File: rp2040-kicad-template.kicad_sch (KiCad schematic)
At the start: 47 parts, among them U1 RP2040, U2 TYPE-C-31-M-12, U3 XC6206PxxxMR, U5 USB Boot, U6 Reset, U7 W25Q16JVUXIQ, U8 PJ-320A, Y1 12MHz - 20pF

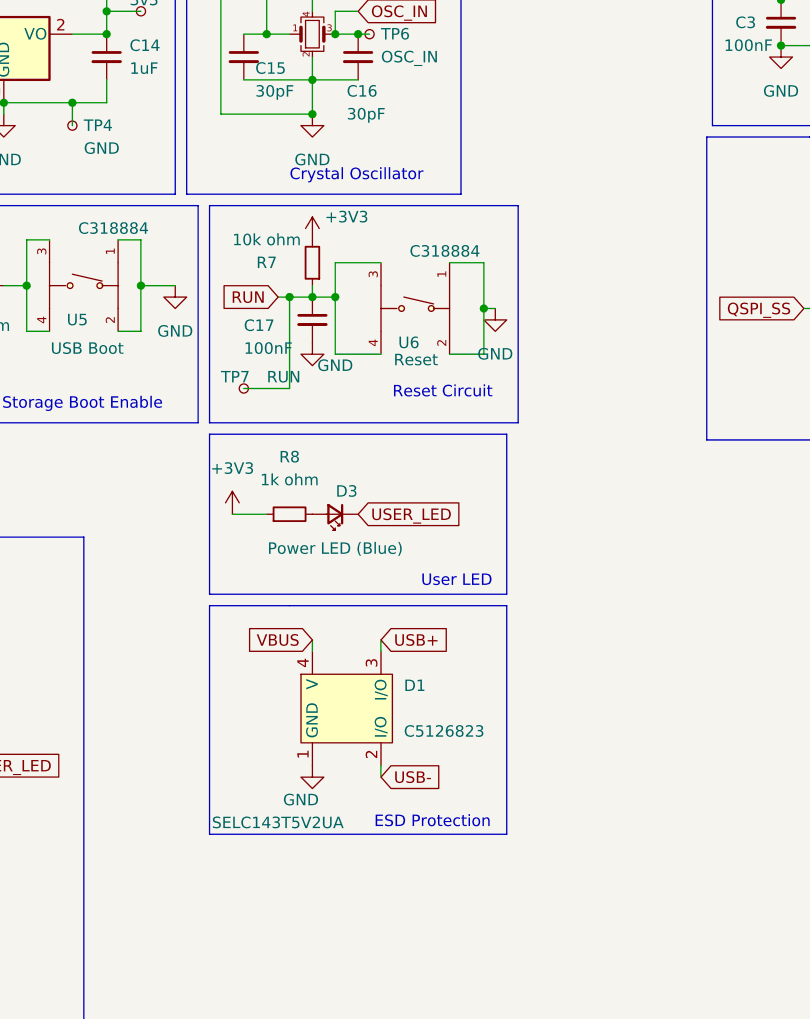
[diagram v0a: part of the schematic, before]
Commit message: Add a different ESD protection unit
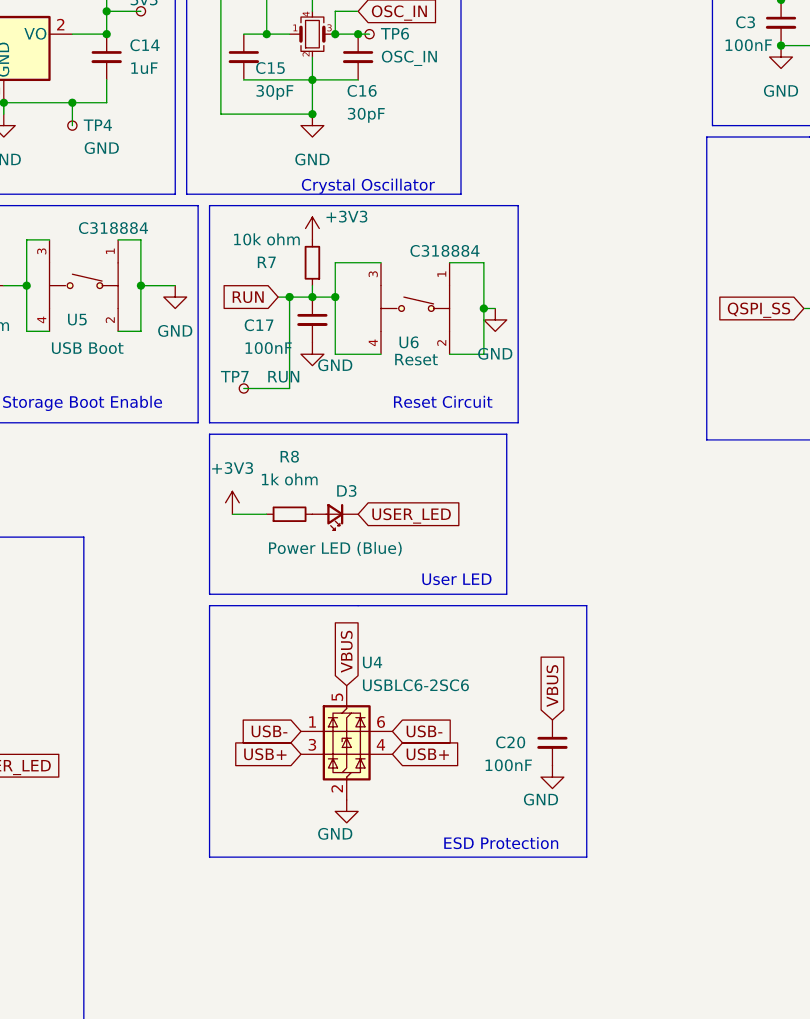
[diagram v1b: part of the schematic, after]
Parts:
- removed D1: SELC143T5V2UA, Package_TO_SOT_SMD:SOT-143, symbol usb_2_esd_protection:SELC143T5V2UA
- added C20: 100nF, Capacitor_SMD:C_0402_1005Metric, symbol Device:C_Small
- added U4: USBLC6-2SC6, Package_TO_SOT_SMD:SOT-23-6, symbol Power_Protection:USBLC6-2SC6
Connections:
- net GND: now also C20.2, U4.2 (GND)
- net USB+: now also U4.3 (I/O2), U4.4 (I/O2)
- net USB-: now also U4.1 (I/O1), U4.6 (I/O1)
- net VBUS: now also C20.1, U4.5 (VBUS)

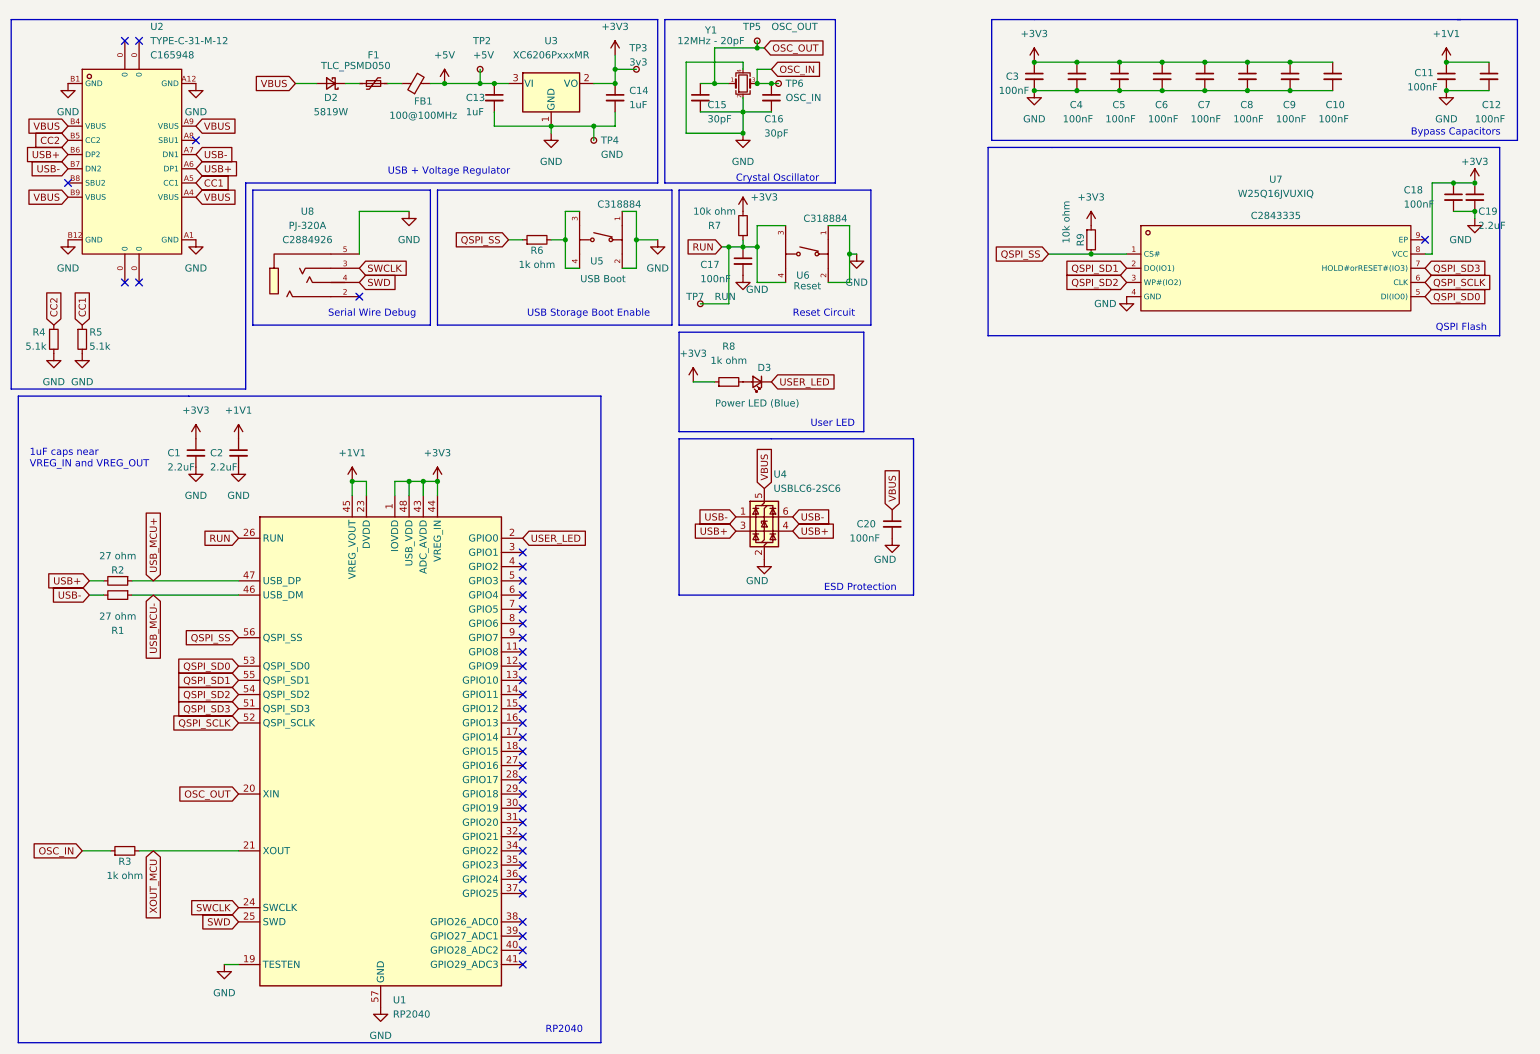
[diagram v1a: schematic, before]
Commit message: Move the RP2040 and associated components to a separate schematic sheet
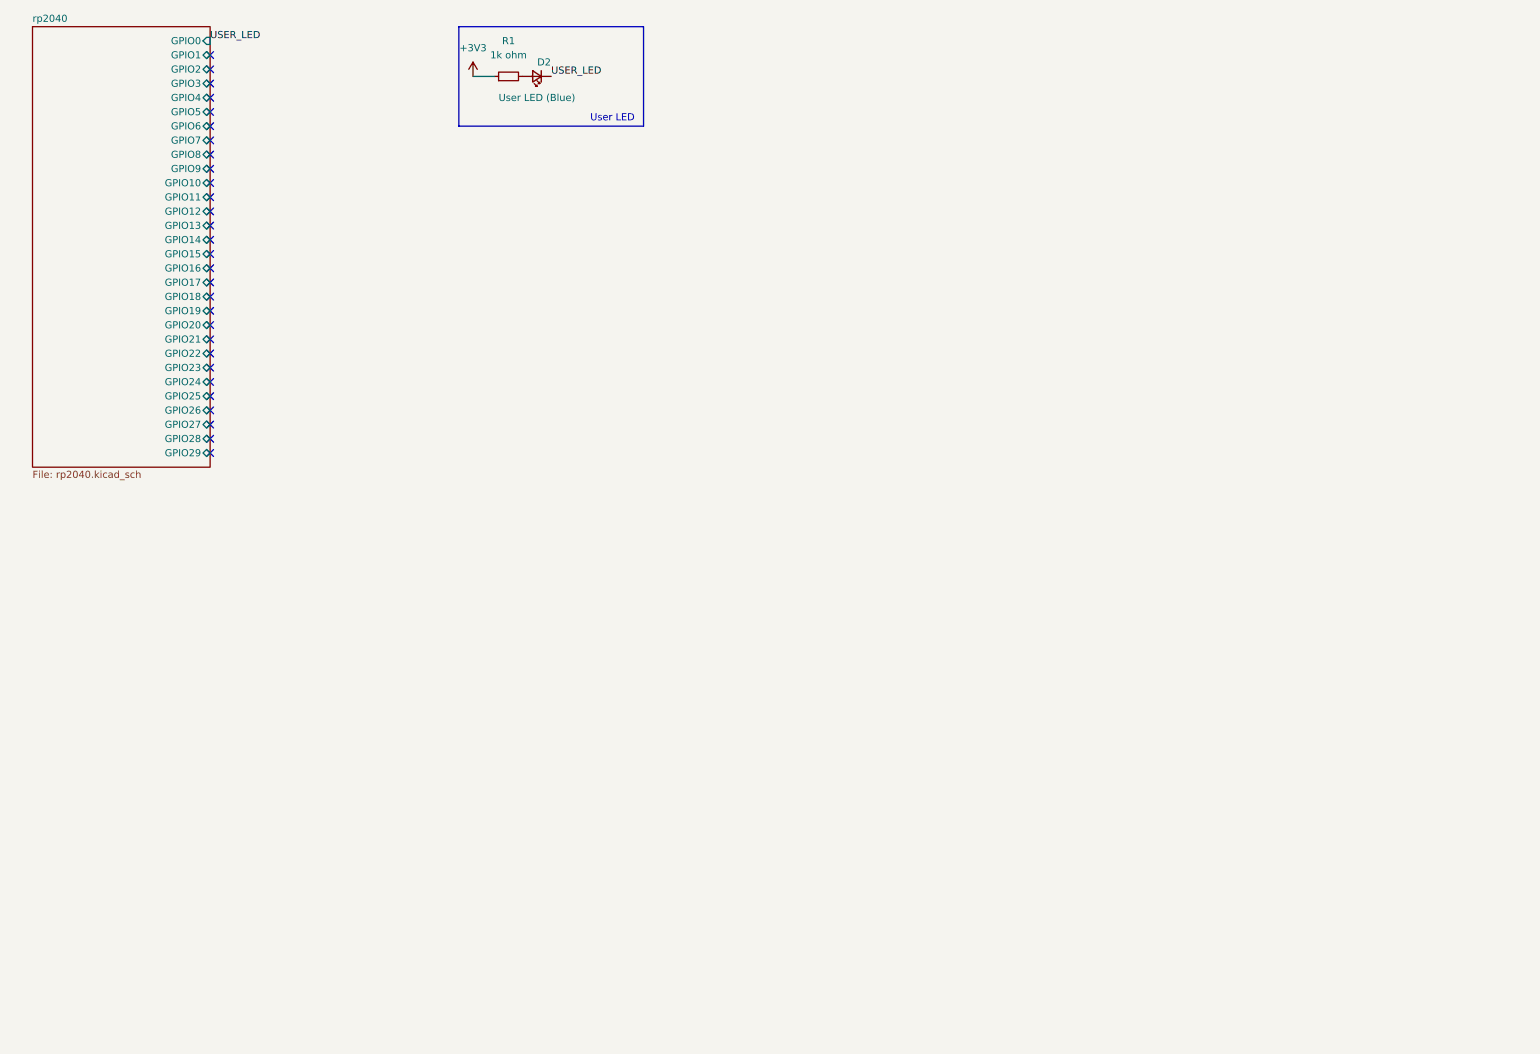
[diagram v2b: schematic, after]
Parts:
- removed C1, C19, C2: 2.2uF, Capacitor_SMD:C_0603_1608Metric, symbol Device:C_Small
- removed C10, C11, C12, C17, C18, C20, C3, C4, C5, C6, C7, C8, C9: 100nF, Capacitor_SMD:C_0402_1005Metric, symbol Device:C_Small
- removed C13, C14: 1uF, Capacitor_SMD:C_0402_1005Metric, symbol Device:C_Small
- removed C15, C16: 30pF, Capacitor_SMD:C_0603_1608Metric, symbol Device:C_Small
- removed D2: 5819W, Diode_SMD:D_SOD-123, symbol Device:D_Schottky_Small
- removed D3: Power LED (Blue), LED_SMD:LED_0805_2012Metric, symbol Device:LED_Small
- removed F1: TLC_PSMD050, Fuse:Fuse_0805_2012Metric, symbol Device:Polyfuse_Small
- removed FB1: 100@100MHz, Inductor_SMD:L_0805_2012Metric, symbol Device:FerriteBead_Small
- removed R2: 27 ohm, Resistor_SMD:R_0603_1608Metric, symbol Device:R_Small
- removed R3, R6, R8: 1k ohm, Resistor_SMD:R_0603_1608Metric, symbol Device:R_Small
- removed R4, R5: 5.1k, Resistor_SMD:R_0603_1608Metric, symbol Device:R_Small
- removed R7, R9: 10k ohm, Resistor_SMD:R_0603_1608Metric, symbol Device:R_Small
- removed TP2: +5V, TestPoint:TestPoint_Pad_D1.0mm, symbol Connector:TestPoint_Small
- removed TP3: 3v3, TestPoint:TestPoint_Pad_D1.0mm, symbol Connector:TestPoint_Small
- removed TP4: GND, TestPoint:TestPoint_Pad_D1.0mm, symbol Connector:TestPoint_Small
- removed TP5: OSC_OUT, TestPoint:TestPoint_Pad_D1.0mm, symbol Connector:TestPoint_Small
- removed TP6: OSC_IN, TestPoint:TestPoint_Pad_D1.0mm, symbol Connector:TestPoint_Small
- removed TP7: RUN, TestPoint:TestPoint_Pad_D1.0mm, symbol Connector:TestPoint_Small
- removed U1: RP2040, Package_DFN_QFN:QFN-56-1EP_7x7mm_P0.4mm_EP3.2x3.2mm, symbol MCU_RaspberryPi:RP2040
- removed U2: TYPE-C-31-M-12, footprints:simple-usb-c, symbol simple-usb-c:TYPE-C-31-M-12
- removed U3: XC6206PxxxMR, Package_TO_SOT_SMD:SOT-23-3, symbol Regulator_Linear:XC6206PxxxMR
- removed U4: USBLC6-2SC6, Package_TO_SOT_SMD:SOT-23-6, symbol Power_Protection:USBLC6-2SC6
- removed U5: USB Boot, footprints:tactile-switch, symbol tactile-switch:TS-1187A-B-A-B
- removed U6: Reset, footprints:tactile-switch, symbol tactile-switch:TS-1187A-B-A-B
- removed U7: W25Q16JVUXIQ, footprints:w25q16jvuxiq, symbol w25q16jvuxiq:W25Q16JVUXIQ
- removed U8: PJ-320A, footprints:trrs-connector-pj320a, symbol trrs-connector-pj320a:PJ-320A
- removed Y1: 12MHz - 20pF, Crystal:Crystal_SMD_3225-4Pin_3.2x2.5mm, symbol Device:Crystal_GND24_Small
- added D2: User LED (Blue), LED_SMD:LED_0805_2012Metric, symbol Device:LED_Small
- R1: value 27 ohm -> 1k ohm; LCSC C25190 -> C21190
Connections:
- net USB_MCU- is gone; now on net +3V3: R1.1
- net USER_LED: now also D2.1 (K)
- net USB-: no longer names the net of R1.2
- net USB-: now also D2.2 (A)
- no-connect marks 37 -> 29
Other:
- added sheet rp2040 (rp2040.kicad_sch)
- note removed: "1uF caps near VREG_IN and VREG_OUT"
- note removed: "Bypass Capacitors"
- note removed: "Crystal Oscillator"
- note removed: "ESD Protection"
- note removed: "QSPI Flash"
- note removed: "RP2040"
- note removed: "Reset Circuit"
- note removed: "Serial Wire Debug"
- note removed: "USB + Voltage Regulator"
- note removed: "USB Storage Boot Enable"

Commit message: Use more 0402 footprints for passive components
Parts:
- R1: footprint Resistor_SMD:R_0603_1608Metric -> Resistor_SMD:R_0402_1005Metric; LCSC C21190 -> C11702
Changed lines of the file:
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@@
 			)
 		)
-		(property "Footprint" "Resistor_SMD:R_0603_1608Metric"
+		(property "Footprint" "Resistor_SMD:R_0402_1005Metric"
 			(at 102.87 24.13 0)
 			(effects
@@
 			)
 		)
-		(property "LCSC" "C21190"
+		(property "LCSC" "C11702"
 			(at 102.87 24.13 90)
 			(effects
